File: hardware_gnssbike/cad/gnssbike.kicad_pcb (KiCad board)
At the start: 4 copper layers, 55 x 97 mm, 117 parts, among them J101 Molex 2036150003, J102 JST SM06B-GHS-TB, J103 contato de mola, 2 vias, J104 contato de mola, 2 vias, J105 contato de mola, 2 vias, J201 Tag-Connect TC2030-NL, J302 contato de mola, 2 vias, J401 Hirose FH28-10S-0.5SH, J402 Molex 503480-0500, Q401 DMG1012T-7, Q601 DMG1012T-7, Q602 DMG1012T-7, Q603 DMG1012T-7, SW601 Omron B3S-1002P, SW602 Omron B3S-1002P, SW603 Omron B3S-1002P, U101 nPM1300-QEAA, U102 MAX17262REWL, U103 AEM10900, U104 TPS7A0218PDQN, U201 MinewSemi ME54BS13, U301 u-blox MAX-F10S, U302 TI TXU0204BQAR, U501 MX25R6435F, U502 Bosch BMP585, U503 Bosch BMI270, U504 MMC5633NJL, U505 TI OPT3001DNPR

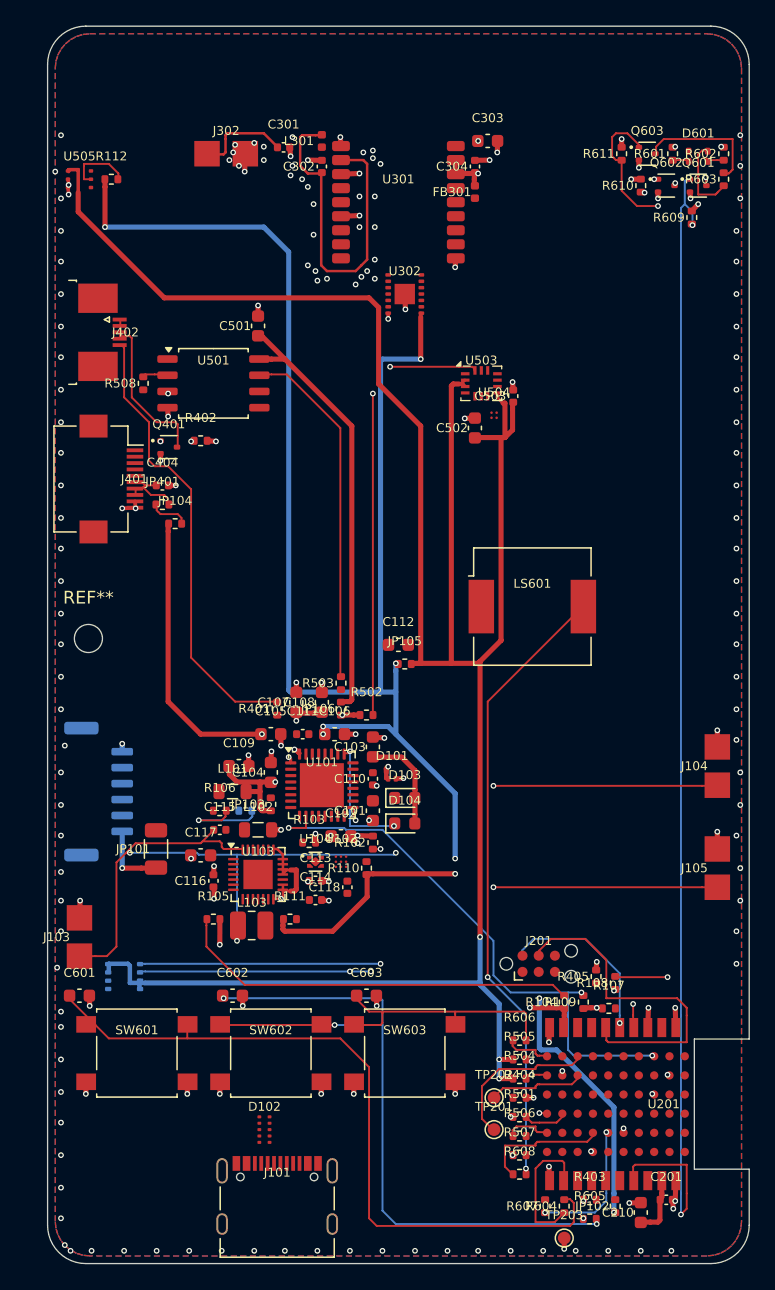
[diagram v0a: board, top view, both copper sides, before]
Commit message: feat(hardware): size the board from the circuit, not from the case
The 55 x 97 mm outline was typed by hand in make_dxf.py and justified by
the inside of the enclosure, and the whole floorplan was absolute
rectangles in that frame - two of them the SHADOWS of the display and the
battery, parts of the case deciding where the board could have a
component. None of that holds: the board's size comes from the circuit and
the case's from the display, the battery and the hand, and shrinking one
does not shrink the other.

The outline is derived now, and one rule dominates: 7.2 of the ME54BS13
datasheet asks 50 mm between two radio modules on the same board, and this
board has two. Sweeping every whole millimetre that clears it and still
fits the row of three keys across the width, the smallest outline with any
margin is 34 x 90: 3060 mm2 against 5335, 43% less board, with the
courtyard occupancy going from 28% to 48%. The two extra millimetres over
the 88 the rule alone allows are not slack - at 88 the receiver had to hug
the left edge to reach the 50 mm, and its own 1V8 pins, which leave on
that side, were left 1.2 mm of board for a capacitor the datasheet wants
within 2.

Three things the squeeze forced, each written where it applies: the key
row left the bottom edge (the module takes 17 of it and the row needs
30.6), the buzzer went to the BACK face (10.5 x 9.5 does not fit the
9.25 mm band left on the front, and pushed out it parked 0.84 mm from the
TPS7A02 and took the ring its decoupling needed), and the GNSS receiver
turned 180 degrees (at 0 the RF_IN pin came out facing the edge 1.2 mm
away, and the pi network sat 10.5 mm from a pin the datasheet wants it
"as short as possible" from).

The placer also stopped treating the two faces as one area. A part on the
back does not take room from a part on the front, and pretending it does
is how a small board runs out of space it has. A part whose pads pierce
the board still takes both, and has to clear both when IT is plac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
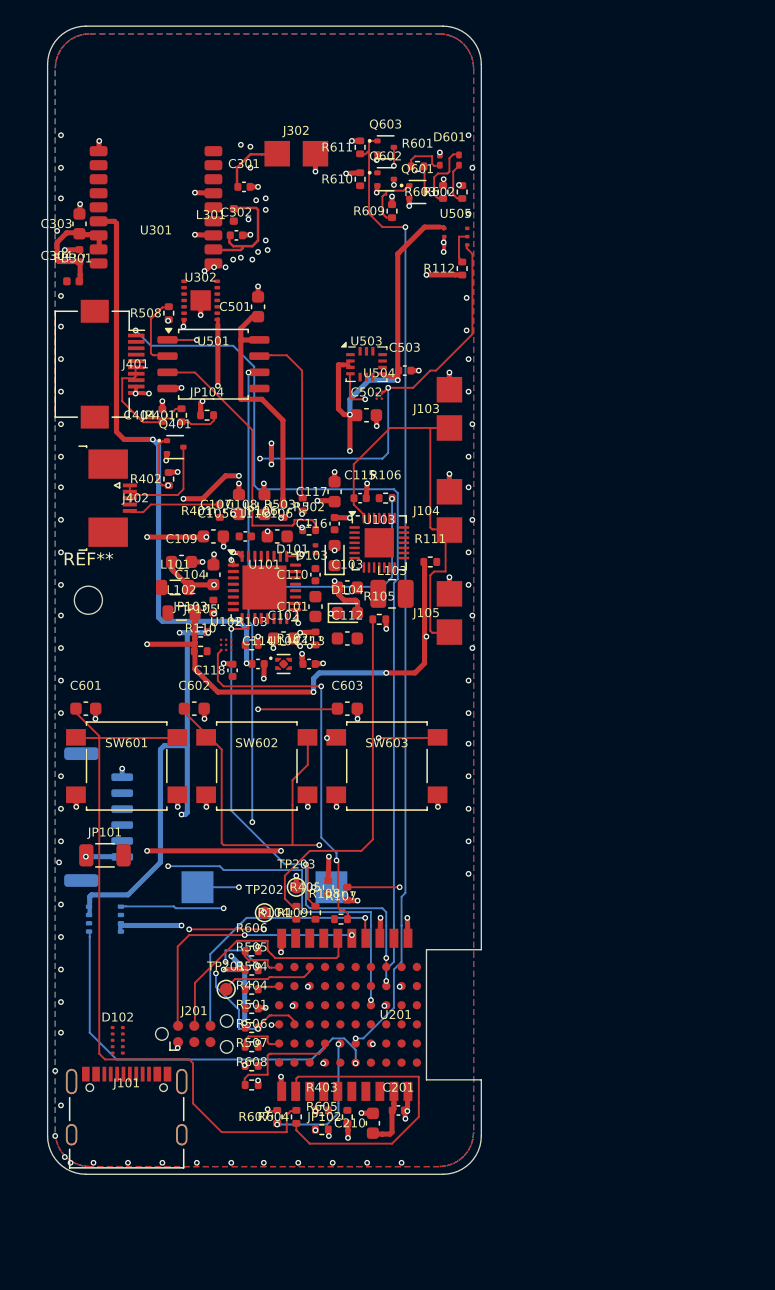
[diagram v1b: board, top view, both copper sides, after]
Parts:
- LS601: footprint Buzzer_Beeper:Buzzer_CUI_CPT-9019S-SMT -> gnssbike:Buzzer_CPT-1117-83-SMT_11x9mm; moved to B.Cu
- moved J103 50.5 mm to (56.5, 55.0)
- moved TP203 34.6 mm to (44.5, 92.5)
- moved C303 32.7 mm to (27.5, 40.5), turned to 90 degrees
- moved FB301 32.3 mm to (27.0, 45.0), turned to 0 degrees
- moved C304 31.8 mm to (27.5, 43.0)
- moved LS601 30.4 mm to (42.0, 92.5)
- moved C117 30.4 mm to (47.5, 61.5), turned to 90 degrees
- moved R111 30.1 mm to (55.0, 67.0)
- moved U505 29.8 mm to (57.0, 41.5)
- moved C116 29.6 mm to (47.5, 64.0)
- moved J104 29.0 mm to (56.5, 63.0)
- moved J105 29.0 mm to (56.5, 71.0)
- moved R112 28.4 mm to (57.5, 44.0), turned to 90 degrees
- moved C115 28.2 mm to (49.5, 62.0)
- moved L103 28.2 mm to (52.0, 69.5)
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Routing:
- net SENS_SDA: track 93.3 -> 1.71 mm, vias 4 -> 0
- net RGB_R: track 93.2 -> 4.87 mm, vias 3 -> 0
- net DISP_SCK: track 0.00 -> 70.8 mm, vias 0 -> 2
- net SRC: track 102.6 -> 33.1 mm, vias 5 -> 0
- net 3V0_SENS: track 183.5 -> 115.7 mm, vias 3 -> 10
- net NOR_MISO: track 0.00 -> 63.2 mm, vias 0 -> 4
- net NOR_CS: track 3.52 -> 63.0 mm, vias 0 -> 3
- net BL_PWM: track 2.70 -> 60.8 mm, vias 2 -> 3
- net IMU_INT: track 0.00 -> 55.3 mm, vias 0 -> 2
- net NOR_SCK_F: track 0.00 -> 54.0 mm, vias 0 -> 3
- net SENS_SCL: track 37.9 -> 85.1 mm, vias 3 -> 5
- net VBCKP: track 0.00 -> 45.4 mm, vias 0 -> 2
- net 3V0: track 238.7 -> 199.4 mm, vias 15 -> 20
- net VSYS: track 7.93 -> 44.7 mm, vias 0 -> 3
- net BARO_INT: track 0.00 -> 31.8 mm, vias 0 -> 1
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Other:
- board size 55 x 97 mm -> 34 x 90 mm

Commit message: feat(hardware): the test points, a readable silkscreen, and paper that fits
Eleven of the sixteen test points of 06-conectores-e-pontos-de-teste.md were
not on the board. Only the three of the console sheet existed; a rail you
cannot put a probe on is a rail you cannot debug. VBUS, VBUSOUT, VBAT, VSYS,
3V0, 1V8, SD3V0, 3V3BL, VBCKP, VINT and the ground reference are there now,
each beside the thing it measures, and each takes what is LEFT: placed with
the rest of JUNTO they pushed three decoupling capacitors off their rings,
one of them to 4.0 mm from a pin that wants 2. The two that are still
missing are the document's own absences - TP111 measures ST_STO, which the
AEM10900 datasheet does not have, and TP401 measures 5V0, from a regulator
not fitted with the JDI panel. The list lives in parts.TESTE and nets.py
refuses a point that names a net that does not exist.

The silkscreen named nothing. Every reference sat 1.8 mm above its part at
0.7 mm with a 0.1 mm stroke - below the floor every fab publishes - and 37
pairs of designators printed on top of each other. The text is at the fab
minimum now, 0.8 mm with 0.15, and each label is PLACED: candidates around
its own courtyard, nearest first, never over another label and preferably
not over another part's outline. 127 references, 0 overlapping. The mounting
hole's REF** is hidden; it names nothing and was the last label sitting on
another.

Ground: a mesh, not just a hem. Edge stitching keeps the boundary of the
surface pours from becoming a radiating slot and does nothing for the
middle, where a patch of pour that reaches the inner plane through a via
20 mm away is not ground at 2.4 GHz. A 4.0 mm grid of ground vias now
covers the board - under the 6.1 mm that is a tenth of a wavelength in
FR-4 - laid last, on what is free, so a stitch never costs a connection.

The router's search learned about pad fields. The neck beside a pad existed
only in emitir(), and emitir only ever sees paths the search already found,
so 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
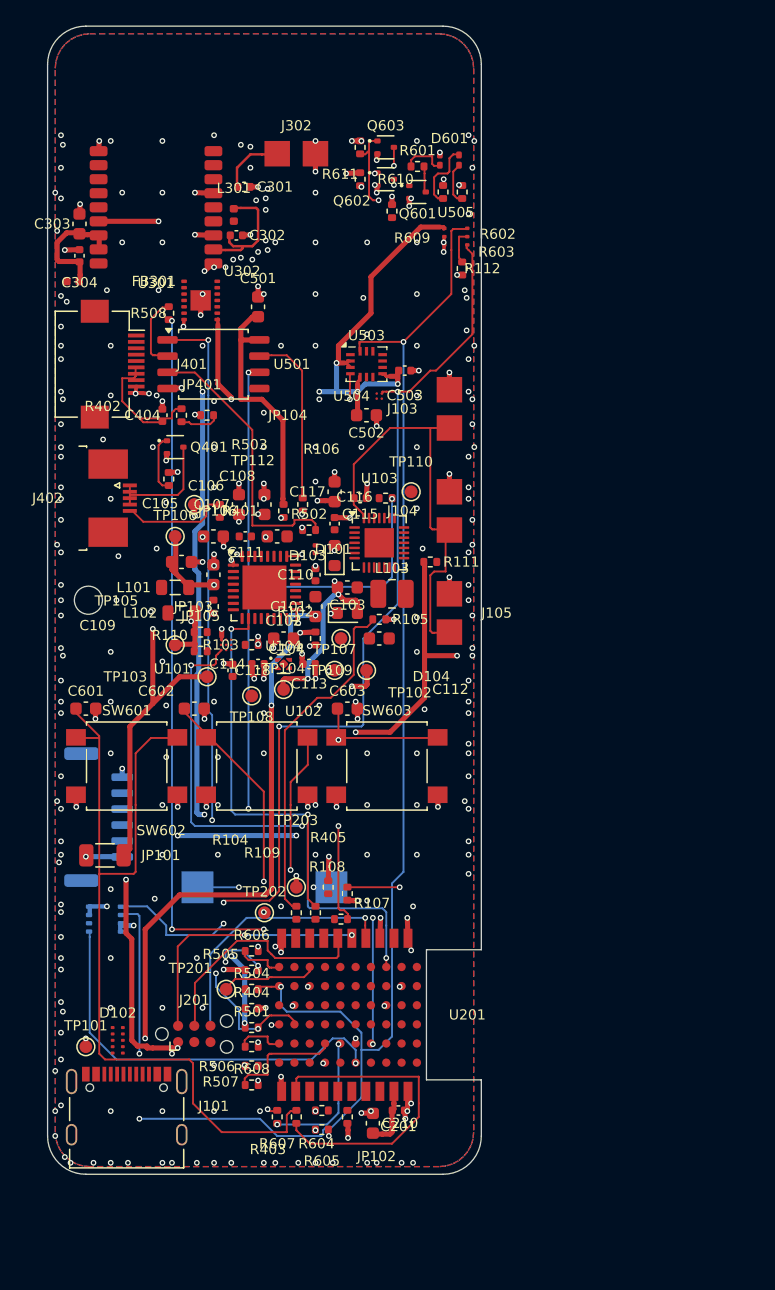
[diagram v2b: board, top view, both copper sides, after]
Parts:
- added TP101: pad, TestPoint:TestPoint_Pad_D1.0mm, F.Cu at (28.0, 105.0)
- added TP102: pad, TestPoint:TestPoint_Pad_D1.0mm, F.Cu at (48.0, 73.0)
- added TP103: pad, TestPoint:TestPoint_Pad_D1.0mm, F.Cu at (37.5, 76.0)
- added TP104: pad, TestPoint:TestPoint_Pad_D1.0mm, F.Cu at (43.5, 77.0)
- added TP105: pad, TestPoint:TestPoint_Pad_D1.0mm, F.Cu at (35.0, 73.5)
- added TP106: pad, TestPoint:TestPoint_Pad_D1.0mm, F.Cu at (35.0, 65.0)
- added TP107: pad, TestPoint:TestPoint_Pad_D1.0mm, F.Cu at (47.5, 75.5)
- added TP108: pad, TestPoint:TestPoint_Pad_D1.0mm, F.Cu at (41.0, 77.5)
- added TP109: pad, TestPoint:TestPoint_Pad_D1.0mm, F.Cu at (50.0, 75.5)
- added TP110: pad, TestPoint:TestPoint_Pad_D1.0mm, F.Cu at (53.5, 61.5)
- added TP112: pad, TestPoint:TestPoint_Pad_D1.0mm, F.Cu at (36.5, 62.5)
- moved C112 2.50 mm to (51.0, 73.0)
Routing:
- net SENS_SDA: track 1.71 -> 125.8 mm, vias 0 -> 4
- net DISP_SCK: track 70.8 -> 0.00 mm, vias 2 -> 0
- net BL_PWM: track 60.8 -> 4.45 mm, vias 3 -> 0
- net VBUS: track 0.00 -> 49.2 mm, vias 0 -> 4
- net VBAT: track 0.00 -> 30.0 mm, vias 0 -> 2
- net VBCKP: track 45.4 -> 65.4 mm, vias 2 -> 3
- net VSYS: track 44.7 -> 55.8 mm, vias 3 -> 5
- net KEY_L_SW: track 57.0 -> 66.9 mm
- net SD3V0: track 45.3 -> 53.4 mm, vias 5 -> 6
- net 3V0_SENS: track 115.7 -> 108.0 mm, vias 10 -> 9
- net KEY_R_SW: track 40.1 -> 33.0 mm, vias 4 -> 2
- net PMIC_INT: track 41.6 -> 47.8 mm
- net PWR_SDA: track 30.2 -> 35.1 mm, vias 2 -> 3
- net RGB_R: track 4.87 -> 0.00 mm
- net 1V8: track 9.82 -> 12.7 mm
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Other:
- board text added: "127 pecas colocadas, 8 fora da placa (painel, antena e modulos solares vivem na caixa)"
- board text added: "GNSS BIKE COMPUTER - placa 34 x 90 mm, 0.8 mm, 4 camadas"
- board text added: "ROTEAMENTO PARCIAL; NADA FABRICADO, NADA MEDIDO"
- board text added: "furo M2 unico; empilhamento assimetrico 0.1 / 0.46 / 0.1 mm, para os 50 ohm da linha de RF"
- board text removed: "116 pecas colocadas, 8 fora da placa (painel, antena e modulos solares vivem na caixa)"
- board text removed: "GNSS BIKE COMPUTER - placa 55 x 97 mm, 0,8 mm, 4 camadas"
- board text removed: "NADA ROTEADO, NADA FABRICADO, NADA MEDIDO"
- board text removed: "furo M2 unico; reparticao do dieletrico PROVISORIA (0,22 mm por vao)"

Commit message: fix(hardware): put the silkscreen where it can be read, in 2D and in 3D
The 3D had no silkscreen at all. kicad-cli's GLB export has no option for
it, so the view showed a green rectangle with parts on it and not one
reference designator - in the picture whose whole job is telling you which
part is which. The SVG export does carry it, and carries it as the simplest
possible thing: 6484 one-segment paths, glyphs included, so no font is
needed and nothing is approximated. Exported over the full page, the SVG's
millimetres are the board file's own coordinates.

Putting it in exposed a bigger error. Measured in the GLB, the substrate
runs z 0 to 0.820 and the copper to 0.855, but this renderer used 0 and
-0.8: every front part was sunk 0.855 mm INTO the board and the silkscreen
was buried under the copper pour, which is why it only ever appeared past
the board edge. Both faces are measured constants now.

The 2D did have the silkscreen, and it was unreadable: KiCad draws it in a
pale cream, and these pages are a filled copper pour in red. It gets two
pages of its own now, front and back, silkscreen only and in black and
white - the assembly drawing, which is the sheet a person uses to find R602
on a board. F.Fab is off them: it carries the library footprint's own copy
of every reference, so each designator printed twice, once large and once
small, on top of itself.

And the "0 overlapping" of the last commit was false. The label width model
was 30% narrow - 0.75 of the text height per character against the 1.06
that KiCad's own textLength measures - so it reported zero while the
exported silkscreen had 35 pairs sitting on each other. Behind that was a
second error: the offset was chosen in the BOARD's frame, and KiCad turns a
footprint property by the footprint's own angle, so a label placed "above" a
part rotated 90 degrees came out beside it. Both fixed, and check_pcb.py now
exports both silkscreen layers and counts the overlaps in KiCad's own
rectangles, with each tex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
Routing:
- net RF_IN: track 10.0 -> 2.31 mm
- net RF_ANT: track 5.08 -> 10.5 mm
- net GND: vias 289 -> 285
